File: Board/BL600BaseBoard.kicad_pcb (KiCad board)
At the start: 2 copper layers, 44.5 x 27.9 mm, 11 parts, among them P1 CONN_17, P2 CONN_4, P3 CONN_17, T1 CONN_1, T2 CONN_1, U1 BL600

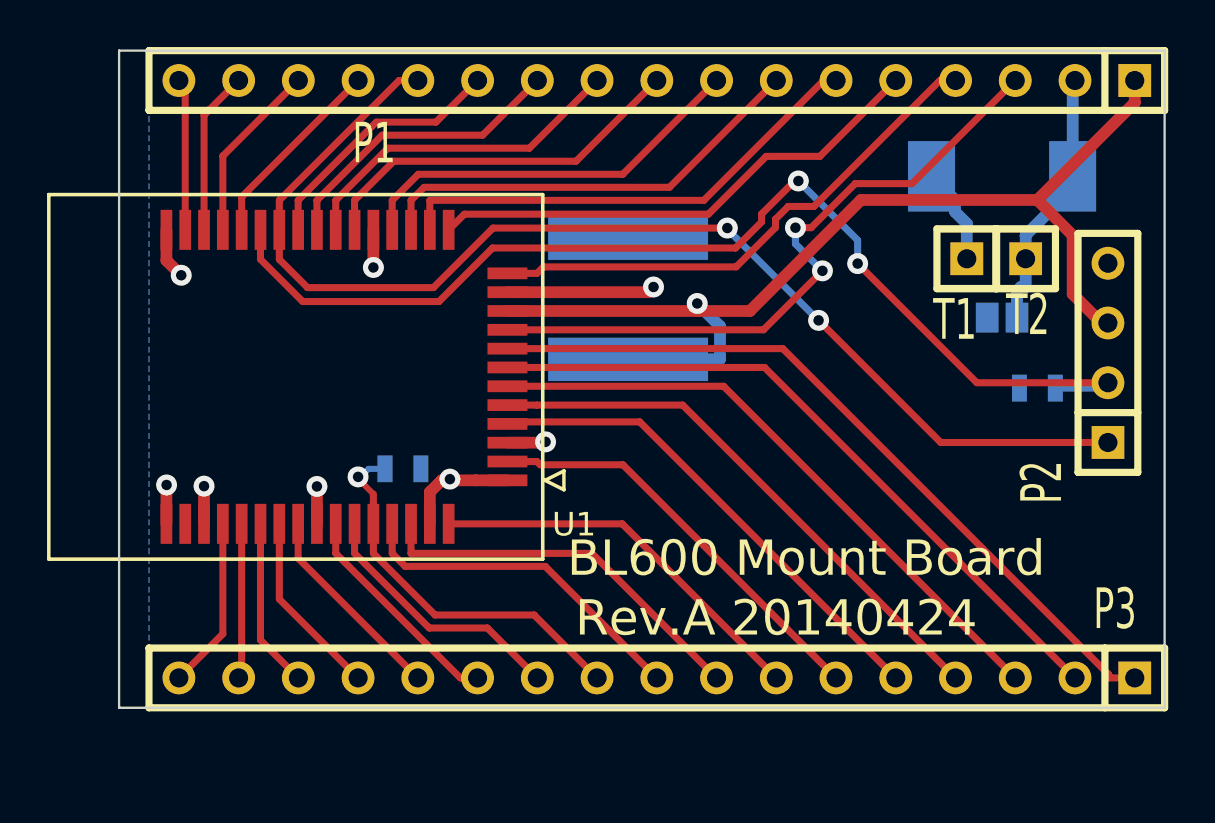
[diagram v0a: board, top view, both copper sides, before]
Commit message: ベースボードに半田付け時のリファレンスピン用穴を追加
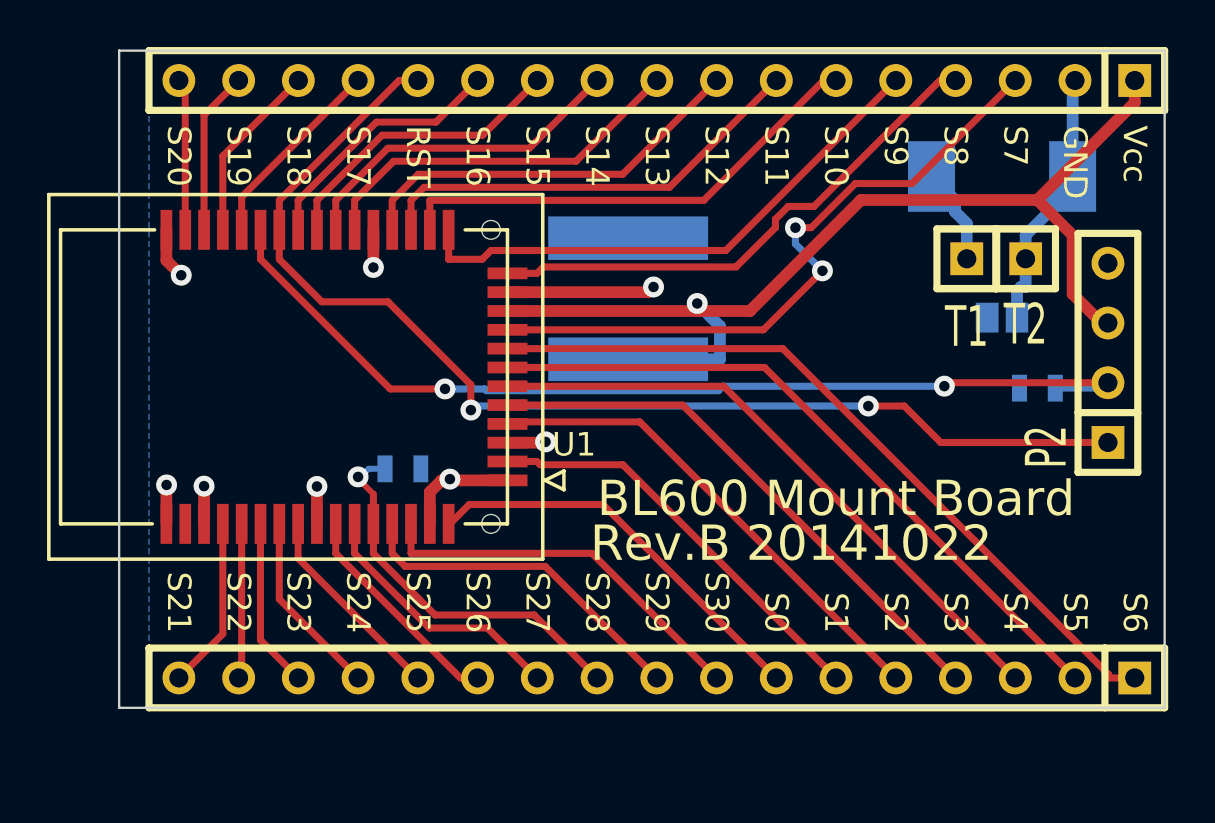
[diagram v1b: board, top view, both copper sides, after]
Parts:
- U1: footprint BL600 -> BL600:BL600
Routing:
- net /SWDCLK: track 46.8 -> 42.1 mm
- net /SIO_9: track 21.6 -> 23.4 mm
- net /nRESET: track 51.1 -> 49.7 mm
- net /SIO_0: track 16.6 -> 17.3 mm
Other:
- board text added: "GND"
- board text added: "RST"
- board text added: "Rev.B 20141022"
- board text added: "S0"
- board text added: "S1"
- board text added: "S10"
- board text added: "S11"
- board text added: "S12"
- board text added: "S13"
- board text added: "S14"
- board text added: "S15"
- board text added: "S16"
- board text added: "S17"
- board text added: "S18"
- board text added: "S19"
- board text added: "S2"
- board text added: "S20"
- board text added: "S21"
- board text added: "S22"
- board text added: "S23"
- board text added: "S24"
- board text added: "S25"
- board text added: "S26"
- board text added: "S27"
- board text added: "S28"
- board text added: "S29"
- board text added: "S3"
- board text added: "S30"
- board text added: "S4"
- board text added: "S5"
- board text added: "S6"
- board text added: "S7"
- board text added: "S8"
- board text added: "S9"
- board text added: "Vcc"
- board text removed: "Rev.A 20140424"

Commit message: Add panelized board cutting path data
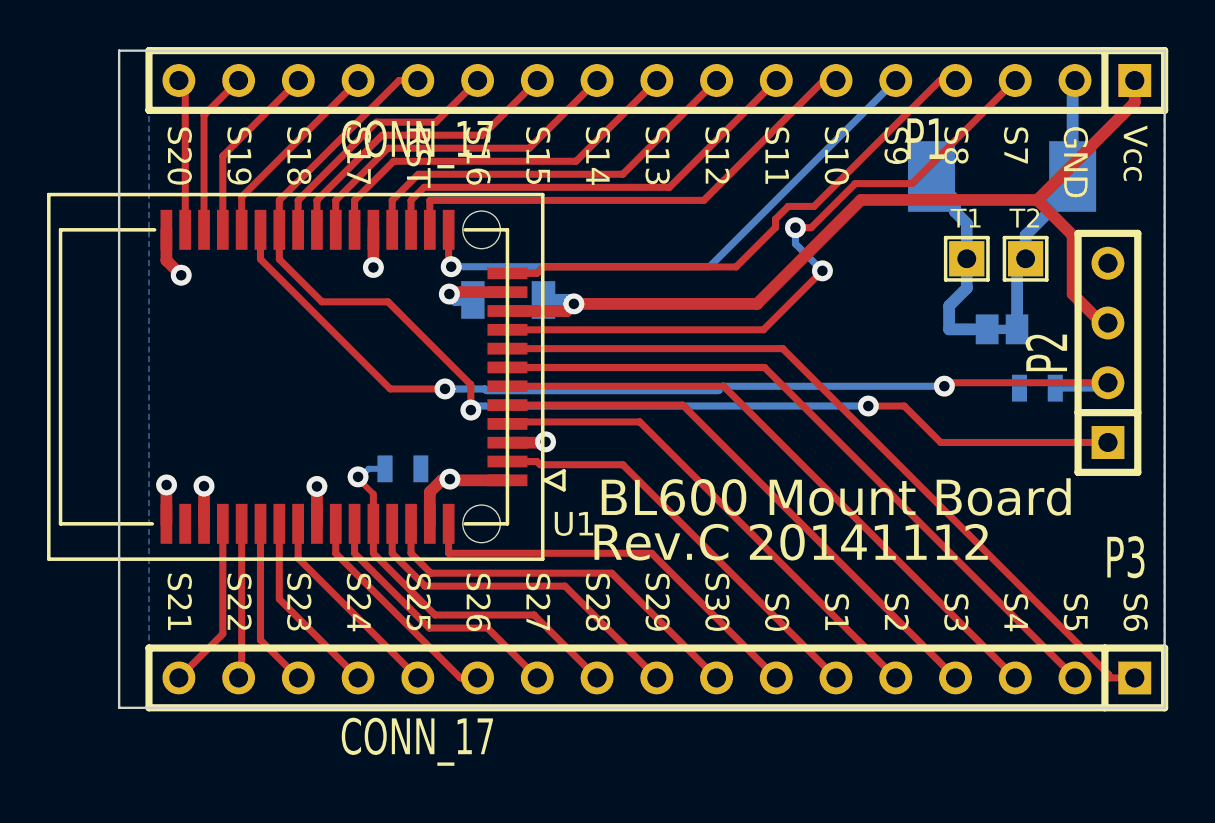
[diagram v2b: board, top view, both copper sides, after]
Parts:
- C1: footprint c_2225 -> Capacitors_SMD:C_1206
- GS1: footprint GS2 -> BL600:GS2_CLOSED
- P1, P3: footprint SIL-17 -> BL600:SIL-17
- P2: footprint SIL-4 -> Connect:SIL-4
- T1, T2: footprint SIL-1 -> Connect:SIL-1
- moved C1 5.10 mm to (141.0, 67.8), turned to 180 degrees
- moved GS1 0.50 mm to (162.0, 69.0)
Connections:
- U1 pad 30: Net-<U1-Pad30> -> (no net)
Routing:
- net /VCC: track 44.9 -> 39.3 mm
- net GND: track 25.6 -> 27.8 mm
- net /GND_CN: track 11.2 -> 12.3 mm
- net /SIO_9: track 23.4 -> 23.8 mm, vias 0 -> 1
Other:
- board text added: "Rev.C 20141112"
- board text removed: "Rev.B 20141022"
